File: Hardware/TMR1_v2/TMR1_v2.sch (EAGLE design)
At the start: 48 parts, among them U1 ATMEGA328P_TQFP, U2 MCP79410I/SN, Y1 32.768kHz

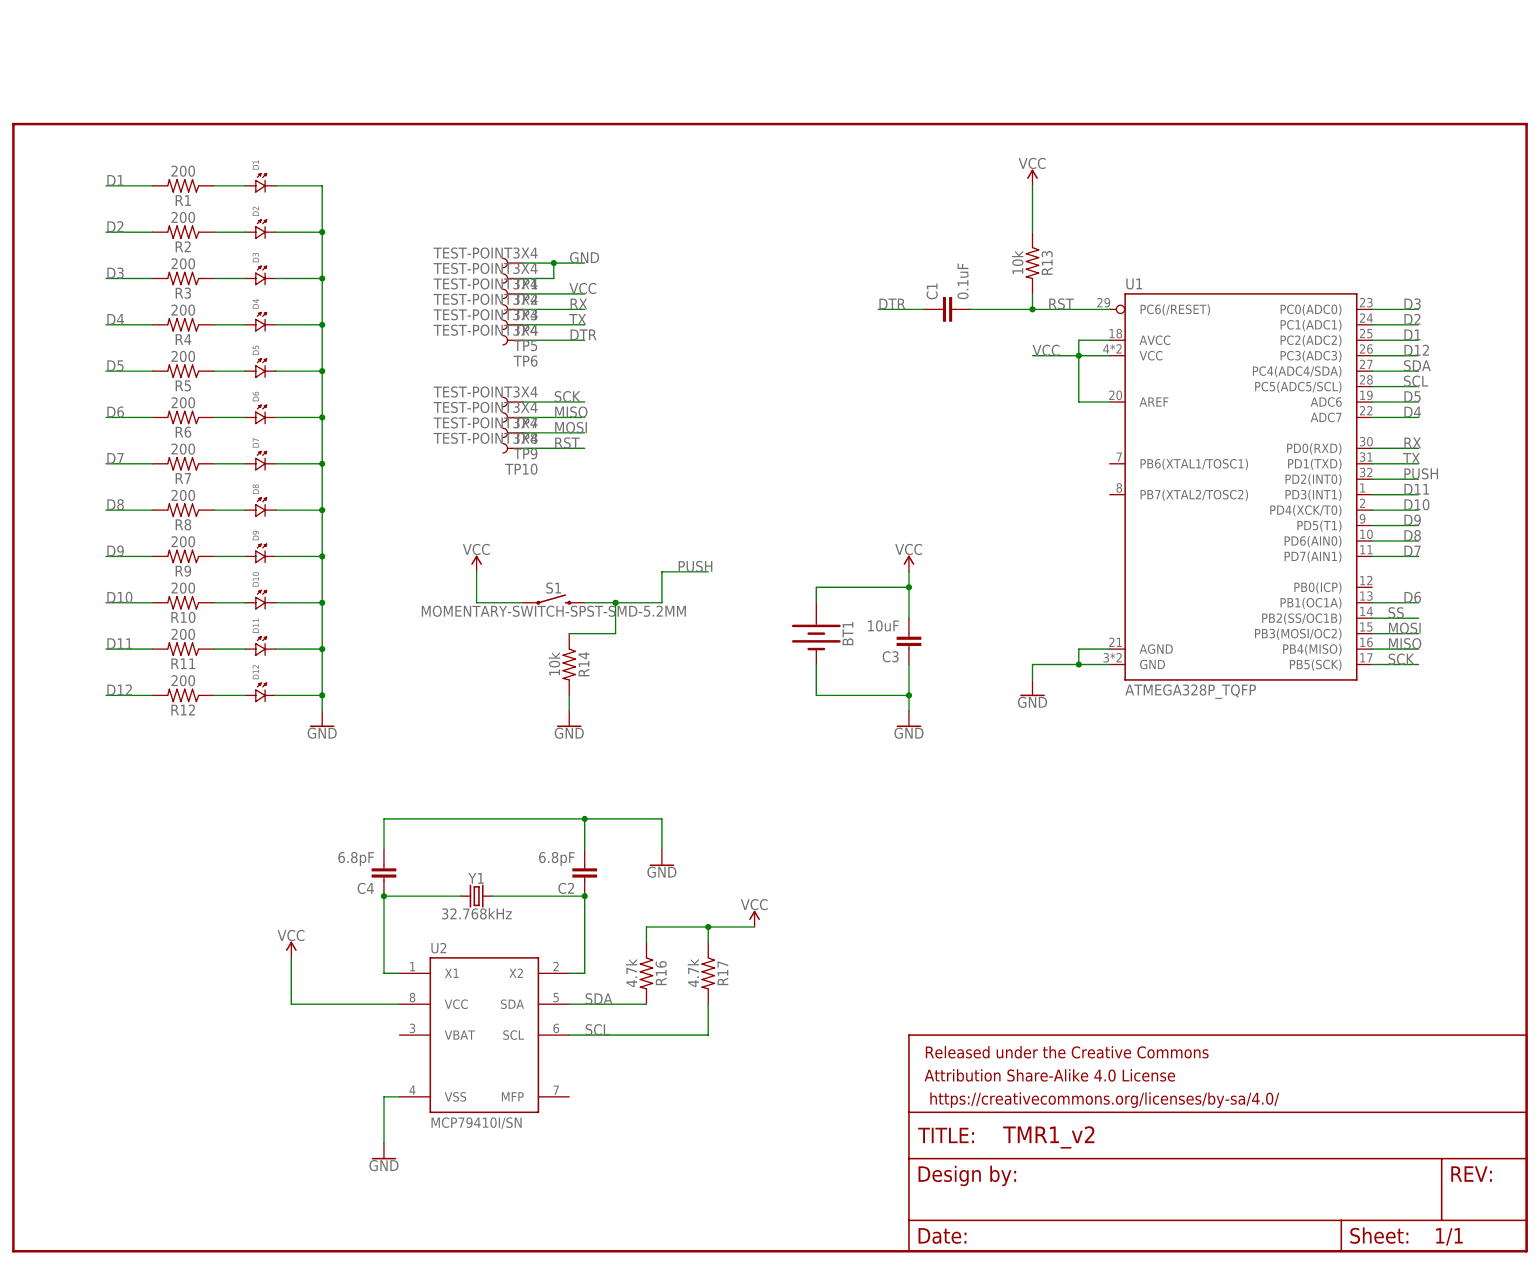
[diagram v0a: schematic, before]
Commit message: HW modifications trying to fit the bora watch.\nSoftware trying the RTC low power version, and atmega with shift register and RTC (possible wall watch)
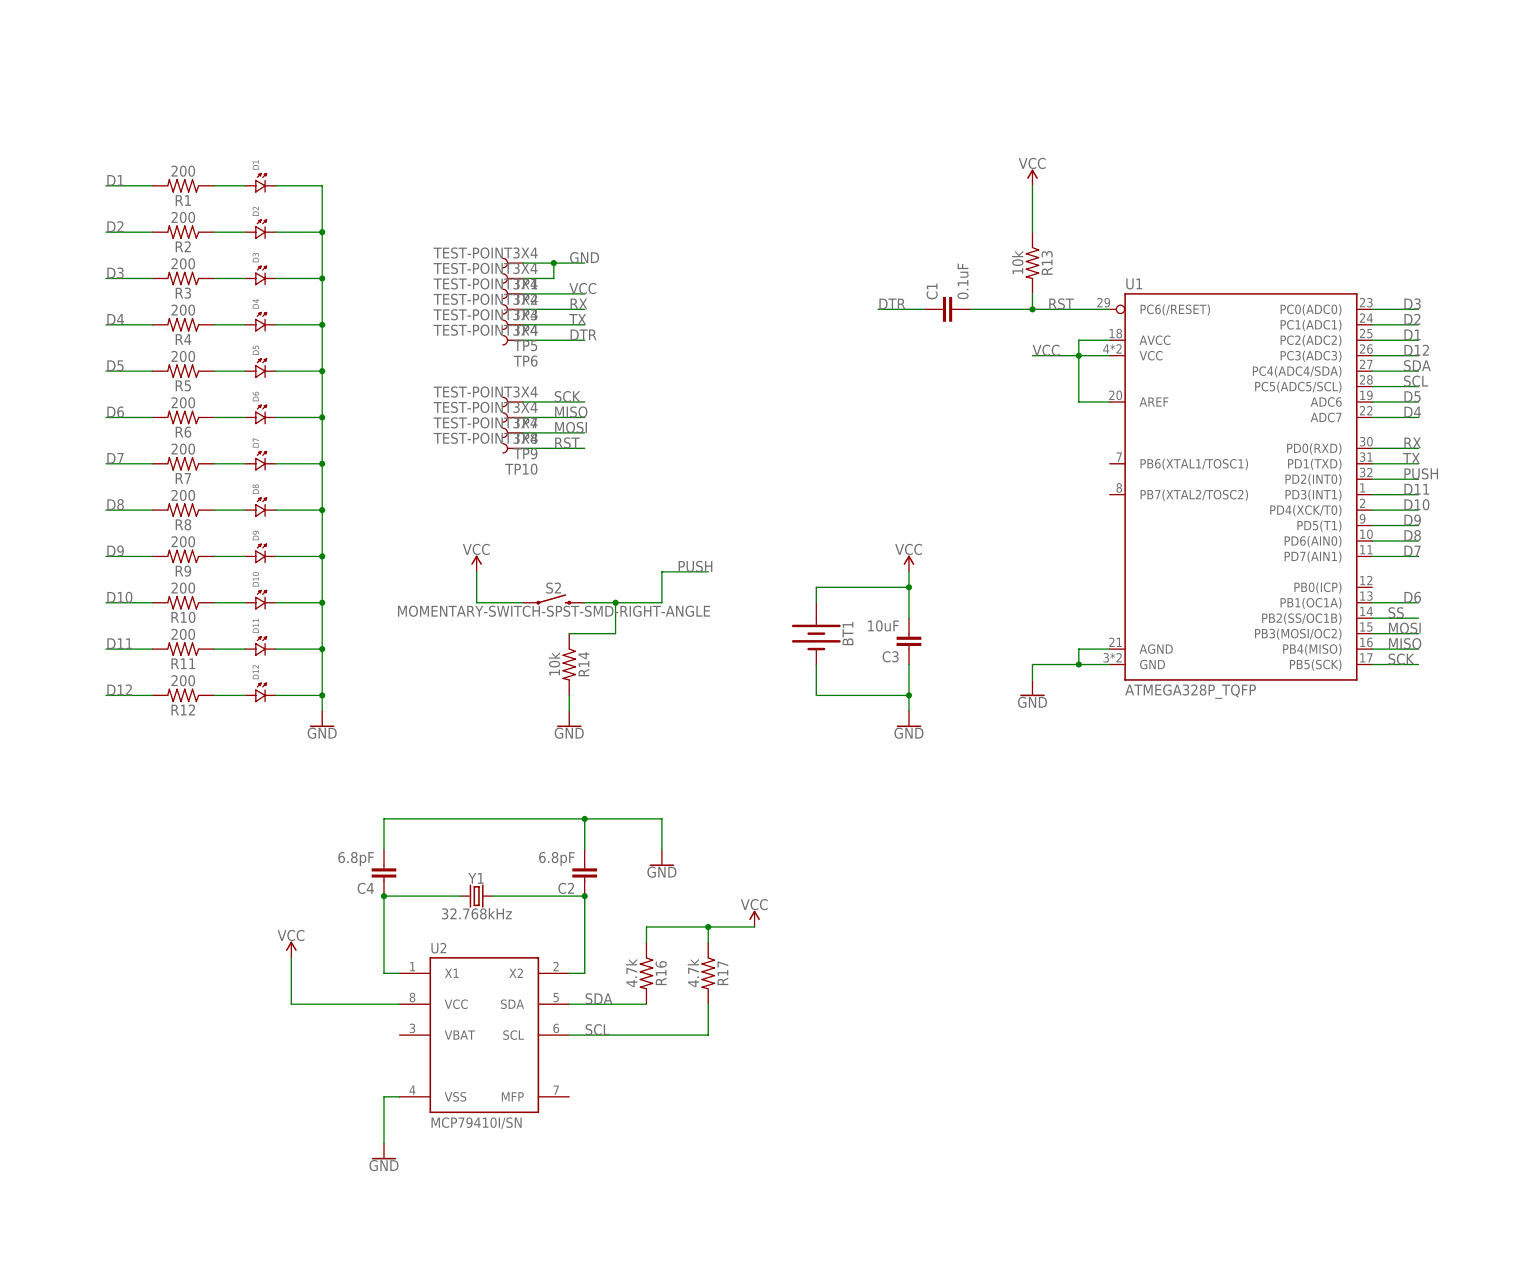
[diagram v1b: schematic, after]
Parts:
- removed FRAME1: FRAME-LETTER, SparkFun-Aesthetics:FRAME-LETTER
- removed S1: MOMENTARY-SWITCH-SPST-SMD-5.2MM, SparkFun-Switches:MOMENTARY-SWITCH-SPST-SMD-5.2MM
- added S2: MOMENTARY-SWITCH-SPST-SMD-RIGHT-ANGLE, SparkFun-Switches:MOMENTARY-SWITCH-SPST-SMD-RIGHT-ANGLE
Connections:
- net PUSH: now also S2.2; no longer S1.2
- net VCC: now also S2.1; no longer S1.1
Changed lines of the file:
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@@
 <setting verticaltext="up"/>
 </settings>
-<grid distance="0.1" unitdist="inch" unit="inch" style="lines" multiple="1" display="no" altdistance="0.01" altunitdist="inch" altunit="inch"/>
+<grid distance="0.1" unitdist="inch" unit="inch" style="lines" multiple="1" display="yes" altdistance="0.01" altunitdist="inch" altunit="inch"/>
 <layers>
 <layer number="1" name="Top" color="4" fill="1" visible="no" active="no"/>
@@
 </classes>
 <parts>
-<part name="FRAME1" library="SparkFun-Aesthetics" deviceset="FRAME-LETTER" device=""/>
 <part name="U1" library="SparkFun-IC-Microcontroller" deviceset="ATMEGA328P_TQFP" device="" value="ATMEGA328P_TQFP"/>
 <part name="C1" library="SparkFun-Capacitors" deviceset="0.1UF" device="-0402-16V-10%" value="0.1uF"/>
@@
 <part name="C3" library="SparkFun-Capacitors" deviceset="10UF" device="-0805-10V-10%" value="10uF"/>
 <part name="R14" library="SparkFun-Resistors" deviceset="RESISTOR" device="0402" value="10k"/>
-<part name="S1" library="SparkFun-Switches" deviceset="MOMENTARY-SWITCH-SPST" device="-SMD-5.2MM"/>
 <part name="SUPPLY3" library="SparkFun-PowerSymbols" deviceset="VCC" device=""/>
 <part name="GND4" library="SparkFun-PowerSymbols" deviceset="GND" device=""/>
@@
 <part name="TP9" library="SparkFun-Connectors" deviceset="TEST-POINT" device="3X4"/>
 <part name="TP10" library="SparkFun-Connectors" deviceset="TEST-POINT" device="3X4"/>
+<part name="S2" library="SparkFun-Switches" deviceset="MOMENTARY-SWITCH-SPST" device="-SMD-RIGHT-ANGLE"/>
 </parts>
 <sheets>
@@
 </plain>
 <instances>
-<instance part="FRAME1" gate="G$1" x="0" y="0"/>
-<instance part="FRAME1" gate="V" x="147.32" y="0">
-<attribute name="LAST_DATE_TIME" x="160.02" y="1.27" size="2.54" layer="94" font="vector"/>
-<attribute name="SHEET" x="233.68" y="1.27" size="2.54" layer="94" font="vector"/>
-<attribute name="DRAWING_NAME" x="162.814" y="17.78" size="2.7432" layer="94" font="vector"/>
-<attribute name="DESIGNER" x="170.434" y="11.176" size="2.7432" layer="94" font="vector"/>
-<attribute name="REV" x="236.22" y="6.604" size="2.7432" layer="94" font="vector"/>
-</instance>
 <instance part="U1" gate="U1" x="203.2" y="124.46">
 <attribute name="NAME" x="182.88" y="158.242" size="1.778" layer="95"/>
@@
 <attribute name="VALUE" x="89.916" y="96.52" size="1.778" layer="96" font="vector" rot="R270" align="top-center"/>
 </instance>
-<instance part="S1" gate="G$1" x="88.9" y="106.68">
-<attribute name="NAME" x="88.9" y="108.204" size="1.778" layer="95" font="vector" align="bottom-center"/>
-<attribute name="VALUE" x="88.9" y="106.172" size="1.778" layer="96" font="vector" align="top-center"/>
-</instance>
 <instance part="SUPPLY3" gate="G$1" x="76.2" y="111.76">
 <attribute name="VALUE" x="76.2" y="114.554" size="1.778" layer="96" align="bottom-center"/>
@@
 <attribute name="NAME" x="86.36" y="129.54" size="1.778" layer="95" font="vector" rot="R180"/>
 <attribute name="VALUE" x="86.36" y="134.62" size="1.778" layer="96" font="vector" rot="R180"/>
+</instance>
+<instance part="S2" gate="G$1" x="88.9" y="106.68">
+<attribute name="NAME" x="88.9" y="108.204" size="1.778" layer="95" font="vector" align="bottom-center"/>
 </instance>
 </instances>
@@
 <segment>
 <pinref part="SUPPLY3" gate="G$1" pin="VCC"/>
-<pinref part="S1" gate="G$1" pin="1"/>
 <wire x1="76.2" y1="111.76" x2="76.2" y2="106.68" width="0.1524" layer="91"/>
 <wire x1="76.2" y1="106.68" x2="83.82" y2="106.68" width="0.1524" layer="91"/>
+<pinref part="S2" gate="G$1" pin="1"/>
 </segment>
 <segment>
@@
 <net name="PUSH" class="0">
 <segment>
-<pinref part="S1" gate="G$1" pin="2"/>
 <wire x1="93.98" y1="106.68" x2="99.06" y2="106.68" width="0.1524" layer="91"/>
 <wire x1="99.06" y1="106.68" x2="106.68" y2="106.68" width="0.1524" layer="91"/>
@@
 <wire x1="99.06" y1="101.6" x2="99.06" y2="106.68" width="0.1524" layer="91"/>
 <junction x="99.06" y="106.68"/>
-</segment>
-<segment>
+<pinref part="S2" gate="G$1" pin="2"/>
+</segment>
+<segment>

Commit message: std easy schematic with all elements in board before route
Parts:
- removed R17: 4.7k, SparkFun-Resistors:RESISTOR0402
- removed S2: MOMENTARY-SWITCH-SPST-SMD-RIGHT-ANGLE, SparkFun-Switches:MOMENTARY-SWITCH-SPST-SMD-RIGHT-ANGLE
- added R15: 10k, SparkFun-Resistors:10KOHM-0603-1/10W-1%
- added S1: MOMENTARY-SWITCH-SPST-SMD-5.2MM, SparkFun-Switches:MOMENTARY-SWITCH-SPST-SMD-5.2MM
- added TP11, TP12: TEST-POINT3X4, SparkFun-Connectors:TEST-POINT3X4
- C2, C4: value 6.8pF -> 22pF; device SparkFun-Capacitors:0.1UF-0402-16V-10% -> SparkFun-Capacitors:22PF-0603-50V-5%
- C3: value 10uF -> 100nF
- D1, D10, D11, D12, D2, D3, D4, D5, D6, D7, D8, D9: device standardparts:LED.0402 -> SparkFun-LED:LED0603
- R1, R10, R11, R12, R2, R3, R4, R5, R6, R7, R8, R9: value 200 -> 330; device SparkFun-Resistors:RESISTOR0402 -> SparkFun-Resistors:330OHM-0603-1/10W-1%
- R13, R14: device SparkFun-Resistors:RESISTOR0402 -> SparkFun-Resistors:10KOHM-0603-1/10W-1%
- R16: value 4.7k -> 10k; device SparkFun-Resistors:RESISTOR0402 -> SparkFun-Resistors:10KOHM-0603-1/10W-1%
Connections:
- net D1: now also R1.1; no longer R1.2
- net D10: now also R10.1; no longer R10.2
- net D11: now also R11.1; no longer R11.2
- net D12: now also R12.1; no longer R12.2
- net D2: now also R2.1; no longer R2.2
- net D3: now also R3.1; no longer R3.2
- net D4: now also R4.1; no longer R4.2
- net D5: now also R5.1; no longer R5.2
- net D6: now also R6.1; no longer R6.2
- net D7: now also R7.1; no longer R7.2
- net D8: now also R8.1; no longer R8.2
- net D9: now also R9.1; no longer R9.2
- net GND: now also C2.1, C4.1, D1.C, D10.C, D11.C, D12.C, D2.C, D3.C, D4.C, D5.C, D6.C, D7.C, D8.C, D9.C, R15.1, TP12.1; no longer C2.2, C4.2, D1.2, D10.2, D11.2, D12.2, D2.2, D3.2, D4.2, D5.2, D6.2, D7.2, D8.2, D9.2, R14.2
- net MISO: now also TP7.1; no longer TP8.1
- net MOSI: now also TP10.1; no longer TP9.1
- net N$1: now also D8.A, R8.2; no longer D8.1, R8.1
- net N$10: now also C4.2; no longer C2.1
- net N$18: now also D9.A, R9.2; no longer D9.1, R9.1
- net N$2: now also D7.A, R7.2; no longer D7.1, R7.1
- net N$20: now also D10.A, R10.2; no longer D10.1, R10.1
- net N$22: now also D11.A, R11.2; no longer D11.1, R11.1
- net N$24: now also D12.A, R12.2; no longer D12.1, R12.1
- net N$3: now also D6.A, R6.2; no longer D6.1, R6.1
- net N$4: now also D5.A, R5.2; no longer D5.1, R5.1
- net N$5: now also D4.A, R4.2; no longer D4.1, R4.1
- net N$6: now also D3.A, R3.2; no longer D3.1, R3.1
- net N$7: now also D2.A, R2.2; no longer D2.1, R2.1
- net N$8: now also D1.A, R1.2; no longer D1.1, R1.1
- net N$9: now also C2.2; no longer C4.1
- net PUSH: now also R15.2, S1.2; no longer R14.1, S2.2
- net RST: now also R16.1, TP11.1; no longer R13.2, TP10.1
- net SCK: now also TP9.1; no longer TP7.1
- net SCL: now also R13.1; no longer R17.2
- net SDA: now also R14.1; no longer R16.2
- net VCC: now also R13.2, R14.2, R16.2, S1.1, TP8.1; no longer R13.1, R16.1, R17.1, S2.1
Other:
- moved on the sheet: C2, C4, R1, R10, R11, R12, R13, R14, R16, R2, R3, R4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

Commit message: before routing
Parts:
- added J1, J2: 455-1750-1-ND, SparkFun-Connectors:CONN_03
- added J3, J4: (no value), SparkFun-Connectors:CONN_04
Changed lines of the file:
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@@
 <part name="TP11" library="SparkFun-Connectors" deviceset="TEST-POINT" device="3X4"/>
 <part name="TP12" library="SparkFun-Connectors" deviceset="TEST-POINT" device="3X4"/>
+<part name="J1" library="SparkFun-Connectors" deviceset="CONN_03" device="" value="455-1750-1-ND"/>
+<part name="J2" library="SparkFun-Connectors" deviceset="CONN_03" device="" value="455-1750-1-ND"/>
+<part name="J3" library="SparkFun-Connectors" deviceset="CONN_04" device=""/>
+<part name="J4" library="SparkFun-Connectors" deviceset="CONN_04" device=""/>
 </parts>
 <sheets>
@@
 <attribute name="NAME" x="86.36" y="129.54" size="1.778" layer="95" font="vector" rot="R180"/>
 </instance>
+<instance part="J1" gate="J$1" x="83.82" y="193.04">
+<attribute name="VALUE" x="81.28" y="185.674" size="1.778" layer="96" font="vector"/>
+<attribute name="NAME" x="81.28" y="198.628" size="1.778" layer="95" font="vector"/>
+</instance>
+<instance part="J2" gate="J$1" x="96.52" y="193.04">
+<attribute name="VALUE" x="93.98" y="185.674" size="1.778" layer="96" font="vector"/>
+<attribute name="NAME" x="93.98" y="198.628" size="1.778" layer="95" font="vector"/>
+</instance>
+<instance part="J3" gate="G$1" x="121.92" y="193.04">
+<attribute name="VALUE" x="116.84" y="185.674" size="1.778" layer="96" font="vector"/>
+<attribute name="NAME" x="116.84" y="201.168" size="1.778" layer="95" font="vector"/>
+</instance>
+<instance part="J4" gate="G$1" x="139.7" y="193.04">
+<attribute name="VALUE" x="134.62" y="185.674" size="1.778" layer="96" font="vector"/>
+<attribute name="NAME" x="134.62" y="201.168" size="1.778" layer="95" font="vector"/>
+</instance>
 </instances>

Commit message: we may not need RX and TX
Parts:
- C3: device SparkFun-Capacitors:10UF-0805-10V-10% -> SparkFun-Capacitors:22PF-0603-50V-5%
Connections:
- net GND: now also C3.2; no longer C3.1
- net VCC: now also C3.1; no longer C3.2
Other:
- moved on the sheet: C3
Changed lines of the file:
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@@
 <part name="GND3" library="SparkFun-PowerSymbols" deviceset="GND" device=""/>
 <part name="BT1" library="SparkFun-Batteries" deviceset="BATTERY" device="-20MM_SMD_4LEGS"/>
-<part name="C3" library="SparkFun-Capacitors" deviceset="10UF" device="-0805-10V-10%" value="100nF"/>
 <part name="SUPPLY3" library="SparkFun-PowerSymbols" deviceset="VCC" device=""/>
 <part name="GND4" library="SparkFun-PowerSymbols" deviceset="GND" device=""/>
@@
 <part name="J3" library="SparkFun-Connectors" deviceset="CONN_04" device=""/>
 <part name="J4" library="SparkFun-Connectors" deviceset="CONN_04" device=""/>
+<part name="C3" library="SparkFun-Capacitors" deviceset="22PF" device="-0603-50V-5%" value="100nF"/>
 </parts>
 <sheets>
@@
 <attribute name="VALUE" x="127.762" y="101.6" size="1.778" layer="96" font="vector" rot="R270" align="top-center"/>
 </instance>
-<instance part="C3" gate="G$1" x="147.32" y="101.6" rot="R180">
-<attribute name="NAME" x="145.796" y="98.679" size="1.778" layer="95" font="vector" rot="R180"/>
-<attribute name="VALUE" x="145.796" y="103.759" size="1.778" layer="96" font="vector" rot="R180"/>
-</instance>
 <instance part="SUPPLY3" gate="G$1" x="76.2" y="111.76">
 <attribute name="VALUE" x="76.2" y="114.554" size="1.778" layer="96" align="bottom-center"/>
@@
 <attribute name="VALUE" x="134.62" y="185.674" size="1.778" layer="96" font="vector"/>
 <attribute name="NAME" x="134.62" y="201.168" size="1.778" layer="95" font="vector"/>
+</instance>
+<instance part="C3" gate="G$1" x="147.32" y="99.06">
+<attribute name="NAME" x="148.844" y="101.981" size="1.778" layer="95" font="vector"/>
+<attribute name="VALUE" x="148.844" y="96.901" size="1.778" layer="96" font="vector"/>
 </instance>
 </instances>
@@
 <wire x1="132.08" y1="96.52" x2="132.08" y2="91.44" width="0.1524" layer="91"/>
 <wire x1="132.08" y1="91.44" x2="147.32" y2="91.44" width="0.1524" layer="91"/>
-<pinref part="C3" gate="G$1" pin="1"/>
 <wire x1="147.32" y1="91.44" x2="147.32" y2="96.52" width="0.1524" layer="91"/>
 <junction x="147.32" y="91.44"/>
+<pinref part="C3" gate="G$1" pin="2"/>
 </segment>
 <segment>
@@
 <wire x1="132.08" y1="109.22" x2="147.32" y2="109.22" width="0.1524" layer="91"/>
 <junction x="147.32" y="109.22"/>
-<pinref part="C3" gate="G$1" pin="2"/>
-</segment>
-<segment>
+<pinref part="C3" gate="G$1" pin="1"/>
+</segment>
+<segment>
